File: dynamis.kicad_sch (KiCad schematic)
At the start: 189 parts, among them J0 USB_C_Receptacle_USB2.0, SW00_00 SW_Push, SW00_01 SW_Push, SW00_02 SW_Push, SW00_03 SW_Push, SW00_04 SW_Push, SW00_05 SW_Push, SW00_06 SW_Push, SW01_00 SW_Push, SW01_01 SW_Push, SW01_02 SW_Push, SW01_03 SW_Push, SW01_04 SW_Push, SW01_05 SW_Push, SW01_06 SW_Push, SW02_01 SW_Push, SW02_02 SW_Push, SW02_03 SW_Push, SW02_04 SW_Push, SW02_05 SW_Push, SW02_06 SW_Push, SW03_00 SW_Push, SW03_02 SW_Push, SW03_03 SW_Push, SW03_04 SW_Push, SW03_05 SW_Push, SW03_06 SW_Push, SW04_00 SW_Push, SW04_01 SW_Push, SW04_02 SW_Push, SW04_03 SW_Push, SW04_05 SW_Push, SW04_06 SW_Push, SW05_01 SW_Push, SW05_02 SW_Push, SW05_03 SW_Push, SW05_04 SW_Push, SW05_05 SW_Push, SW05_06 SW_Push, SW06_00 SW_Push, SW06_01 SW_Push, SW06_02 SW_Push, SW06_03 SW_Push, SW06_04 SW_Push, SW06_05 SW_Push, SW06_06 SW_Push, SW07_01 SW_Push, SW07_02 SW_Push, SW07_03 SW_Push, SW07_04 SW_Push, SW07_05 SW_Push, SW07_06 SW_Push, SW08_00 SW_Push, SW08_02 SW_Push, SW08_03 SW_Push, SW08_04 SW_Push, SW08_05 SW_Push, SW08_06 SW_Push, SW09_00 SW_Push, SW09_01 SW_Push, SW09_02 SW_Push, SW09_03 SW_Push, SW09_04 SW_Push, SW09_05 SW_Push, SW09_06 SW_Push, U0 ATmega32U4-A, U1 PMW3360DM-T2QU, U2 TLV70019DDCR, U3 74LVC1T45GW,125, U4 74LVC1T45GW,125, U5 74LVC1T45GW,125, U6 74LVC1T45GW,125, U7 74LVC1T45GW,125, Y0 16Mhz

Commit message: wip
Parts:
- added LED5, LED6: WS2812B, LED_SMD:LED_WS2812B_PLCC4_5.0x5.0mm_P3.2mm, symbol LED:WS2812B
- renumbered LED8 to LED10, LED9 to LED11, LED5 to LED7, LED6 to LED8, LED7 to LED9
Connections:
- net GND: now also LED5.3 (VSS), LED6.3 (VSS)
- net VCC: now also LED5.1 (VDD), LED6.1 (VDD)
- net at LED7.4 (DIN): now also LED6.2 (DOUT); no longer LED4.2 (DOUT)
- new net: LED4.2 (DOUT), LED5.4 (DIN)
- new net: LED5.2 (DOUT), LED6.4 (DIN)
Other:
- moved on the sheet: LED0, LED1, LED10, LED11, LED2, LED3, LED4, LED7, LED8, LED9

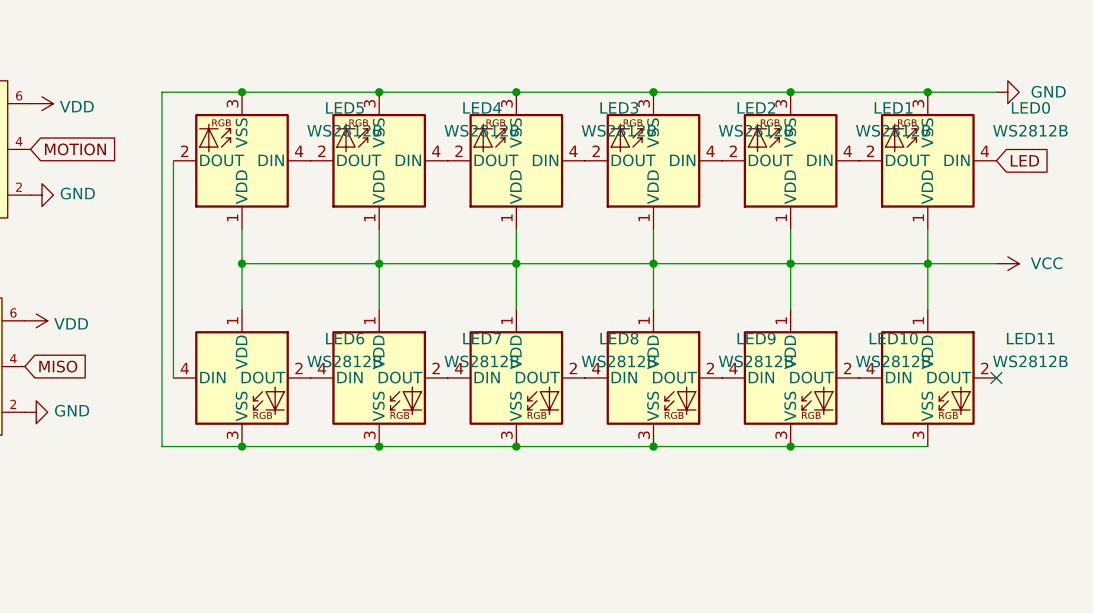
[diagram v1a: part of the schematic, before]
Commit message: mod name of 3dp gasket mount case dir
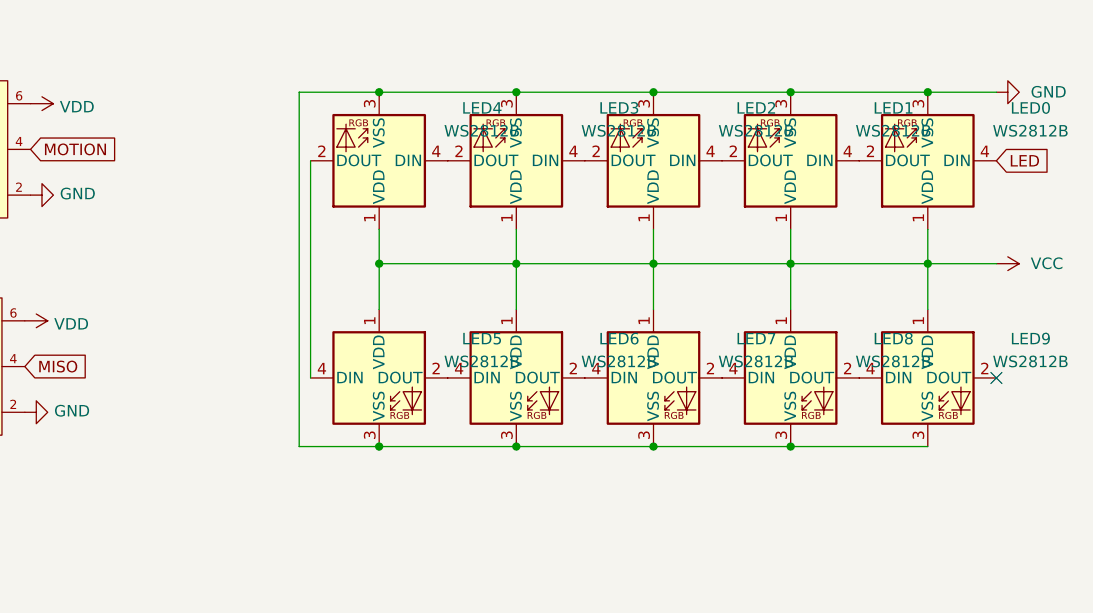
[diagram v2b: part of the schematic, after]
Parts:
- removed LED4, LED7: WS2812B, LED_SMD:LED_WS2812B_PLCC4_5.0x5.0mm_P3.2mm, symbol LED:WS2812B
- SW01_00: footprint MX_Only:MXOnly-1U-Hotswap -> MX_Only:MXOnly-1.5U-Hotswap
- SW03_00, SW04_00, SW04_01, SW04_02, SW04_06, SW09_05, SW09_06, SWSP_S04: footprint MX_Only:MXOnly-1U-Hotswap -> MX_Only:MXOnly-1.25U-Hotswap
- SW04_03: footprint MX_Only:MXOnly-1U-Hotswap -> MX_Only:MXOnly-2.25U-Hotswap-ReversedStabilizers
- SW04_05: footprint MX_Only:MXOnly-1U-Hotswap -> MX_Only:MXOnly-2.75U-Hotswap-ReversedStabilizers
- SWBS_L00: footprint MX_Only:MXOnly-1U-Hotswap -> MX_Only:MXOnly-2U-Hotswap
- SWCL_N00, SWRS_S01: footprint MX_Only:MXOnly-1U-Hotswap -> MX_Only:MXOnly-1.75U-Hotswap
- SWLS_L01: footprint MX_Only:MXOnly-1U-Hotswap -> MX_Only:MXOnly-2.25U-Hotswap
- SWRS_L01: footprint MX_Only:MXOnly-1U-Hotswap -> MX_Only:MXOnly-2.75U-Hotswap
- SWSP_L04: footprint MX_Only:MXOnly-1U-Hotswap -> MX_Only:MXOnly-6.25U-Hotswap
- renumbered LED5 to LED4, LED6 to LED5, LED8 to LED6, LED9 to LED7, LED10 to LED8, LED11 to LED9
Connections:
- net at LED6.4 (DIN): now also LED5.2 (DOUT)
- net at LED4.4 (DIN): now also LED3.2 (DOUT)
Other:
- moved on the sheet: LED4, LED5

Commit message: Develop v2 (#27)
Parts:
- removed C5, C6: 1μF, Capacitor_SMD:C_1206_3216Metric, symbol Device:C
- removed JP0: SJ, Jumper:SolderJumper-2_P1.3mm_Open_Pad1.0x1.5mm, symbol Jumper:SolderJumper_2_Open
- removed LED0, LED1, LED2, LED3, LED4, LED5, LED6, LED7, LED8, LED9: WS2812B, LED_SMD:LED_WS2812B_PLCC4_5.0x5.0mm_P3.2mm, symbol LED:WS2812B
- removed R7, R8: 10k, Resistor_SMD:R_1206_3216Metric, symbol Device:R
- removed U0: ATmega32U4-A, Package_QFP:TQFP-44_10x10mm_P0.8mm, symbol MCU_Microchip_ATmega:ATmega32U4-A
- removed U2: TLV70019DDCR, TLV70019DDCR:Texas_Instruments-TLV70019DDCR-Level_A, symbol TLV70019DDCR:TLV70019DDCR
- removed U3, U4, U5, U6, U7: 74LVC1T45GW,125, 74LVC1T45GW:Nexperia-SOT363-11_2018-0-IPC_A, symbol 74LVC1T45GW:74LVC1T45GW,125
- added C10, C12, C16, C20: 10μF, Capacitor_SMD:C_1206_3216Metric, symbol Device:C
- added C11, C13, C15, C17, C19, C9: 0.1μF, Capacitor_SMD:C_1206_3216Metric, symbol Device:C
- added C14, C18: 1μF, Capacitor_SMD:C_1206_3216Metric, symbol Device:C
- added C21: 4.7μF, Capacitor_SMD:C_1206_3216Metric, symbol Device:C
- added ESDD0: ESD5Z5V0, Diode_SMD:D_SOD-523, symbol Diode:1.5KExxA
- added F0: SMD0805-050-16V, Fuse:Fuse_1206_3216Metric, symbol Device:Fuse
- added LED00, LED01, LED02, LED03, LED04: SK6812MINI-E, SK6812MINI-E:SK6812MINIE, symbol SK6812MINI-E:SK6812MINI-E
- added R10: 63.4K, Resistor_SMD:R_1206_3216Metric, symbol Device:R
- added R11: 52.3k, Resistor_SMD:R_1206_3216Metric, symbol Device:R
- added R12: 30.1k, Resistor_SMD:R_1206_3216Metric, symbol Device:R
- added R13: 1M, Resistor_SMD:R_1206_3216Metric, symbol Device:R
- added R5: 10k, Resistor_SMD:R_1206_3216Metric, symbol Device:R
- added R9: 37.4k, Resistor_SMD:R_1206_3216Metric, symbol Device:R
- added U0: ATmega32U4-M, Package_DFN_QFN:QFN-44-1EP_7x7mm_P0.5mm_EP5.2x5.2mm, symbol MCU_Microchip_ATmega:ATmega32U4-M
- added U2, U3: TPS73601DBV, Package_TO_SOT_SMD:SOT-23-5, symbol Regulator_Linear:TPS73601DBV
- added U4: TPD4E05U06DQAR, TPD4E05U06DQAR:USON-10_L2.5-W1.0-P0.50-BL, symbol random-keyboard-parts:TPD4E05U06DQAR
- C0, C1: LCSC (none) -> C107174
- C2: LCSC (none) -> C1848
- C3: renamed from C7; LCSC (none) -> C24497
- C4: renamed from C8; LCSC (none) -> C24497
- C5: renamed from C9; LCSC (none) -> C24497
- C6: renamed from C10; LCSC (none) -> C13585
- C7: renamed from C3; LCSC (none) -> C29823
- C8: renamed from C4; LCSC (none) -> C24497
- D00_00, D00_01, D00_02, D00_03, D00_04, D00_05, D00_06, D01_00, D01_01, D01_02, D01_03, D01_04, D01_05, D01_06, D02_00, D02_01, D02_02, D02_03, D02_04, D02_05, D02_06, D03_00, D03_01, D03_02, D03_03, D03_04, D03_05, D03_06, D04_00, D04_01, D04_02, D04_03, D04_04, D04_05, D04_06, D05_00, D05_01, D05_02, D05_03, D05_04, D05_05, D05_06, D06_00, D06_01, D06_02, D06_03, D06_04, D06_05, D06_06, D07_00, D07_01, D07_02, D07_03, D07_04, D07_05, D07_06, D08_00, D08_01, D08_02, D08_03, D08_04, D08_05, D08_06, D09_00, D09_01, D09_02, D09_03, D09_04, D09_05, D09_06: LCSC (none) -> C81598
- J0: LCSC (none) -> C165948
- R0, R1: LCSC (none) -> C17958
- R2: LCSC (none) -> C17928
- R3, R4: LCSC (none) -> C964991
- R6: renamed from R5; LCSC (none) -> C17928
- R7: renamed from R6; LCSC (none) -> C286655
- RESET_SW0: LCSC (none) -> C318884
- SW00_00, SW00_01, SW00_02, SW00_03, SW00_04, SW00_05, SW00_06, SW01_00, SW01_01, SW01_02, SW01_03, SW01_04, SW01_05, SW01_06, SW02_01, SW02_02, SW02_03, SW02_04, SW02_05, SW02_06, SW03_00, SW03_02, SW03_03, SW03_04, SW03_05, SW03_06, SW04_00, SW04_01, SW04_02, SW04_03, SW04_05, SW04_06, SW05_01, SW05_02, SW05_03, SW05_04, SW05_05, SW05_06, SW06_00, SW06_01, SW06_02, SW06_03, SW06_04, SW06_05, SW06_06, SW07_01, SW07_02, SW07_03, SW07_04, SW07_05, SW07_06, SW08_00, SW08_02, SW08_03, SW08_04, SW08_05, SW08_06, SW09_00, SW09_01, SW09_02, SW09_03, SW09_04, SW09_05, SW09_06, SWBS_L00, SWBS_S00, SWCL_N00, SWCL_S00, SWET_AN00, SWLS_L01, SWLS_S01, SWRS_L01, SWRS_S01, SWSP_L04, SWSP_S04: LCSC (none) -> C5156480
- SWET_IS00: footprint MX_Only:MXOnly-1U-Hotswap -> MX_Only:MXOnly-2U-Hotswap-ReversedStabilizers; LCSC (none) -> C5156480
- Y0: footprint Crystal:Crystal_SMD_SeikoEpson_FA238-4Pin_3.2x2.5mm -> X322516MLB4SI:OSC-SMD_4P-L3.2-W2.5-BL; LCSC (none) -> C13738
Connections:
- net D+: now also U4.4 (D2+), U4.5 (D2-), U4.6 (NC), U4.7 (NC)
- net D-: now also U4.1 (D1+), U4.10 (NC), U4.2 (D1-), U4.9 (NC)
- net GND: now also C7.2, C8.2, C10.2, C11.2, C12.2, C13.2, C14.2, C16.2, C17.2, C18.2, C20.2, C21.1, C9.2, ESDD0.2 (A2), LED00.3 (GND), LED01.3 (GND), LED02.3 (GND), LED03.3 (GND), LED04.3 (GND), R10.2, R12.2, R13.1, U0.15 (GND), U0.23 (GND), U0.35 (GND), U0.43 (GND), U0.45 (GND), U0.5 (UGND), U2.2 (GND), U3.2 (GND), U4.3 (GND), U4.8 (GND); no longer C7.1, C8.1, J0.S1 (SHIELD)
- net LED: now also LED00.4 (DIN), U0.1 (PE6)
- net MISO: now also U0.11 (PB3)
- net MOSI: now also U0.10 (PB2)
- net MOTION: now also U0.12 (PB7)
- net RESET: now also R5.2, U0.13 (~{RESET})
- net RE_A: now also U0.41 (PF0)
- net RE_B: now also U0.40 (PF1)
- net SCLK: now also U0.9 (PB1)
- net VCC: now also ESDD0.1 (A1), F0.1; no longer C3.1, C4.1, C5.1, C6.1
- net col00: now also U0.18 (PD0)
- net col01: now also U0.19 (PD1)
- net col02: now also U0.37 (PF6)
- net col03: now also U0.36 (PF7)
- net col04: now also U0.22 (PD5)
- net col05: now also U0.39 (PF4)
- net col06: now also U0.38 (PF5)
- net row00: now also U0.25 (PD4)
- net row01: now also U0.26 (PD6)
- net row02: now also U0.27 (PD7)
- net row03: now also U0.21 (PD3)
- net row04: now also U0.20 (PD2)
- net row05: now also U0.31 (PC6)
- net row06: now also U0.30 (PB6)
- net row07: now also U0.29 (PB5)
- net row08: now also U0.28 (PB4)
- net row09: now also U0.32 (PC7)
- net at C2.1: now also U0.6 (UCAP)
- net at C0.2, Y0.3: now also U0.17 (XTAL1)
- net at R0.1: now also U0.4 (D+)
- net at C1.1, Y0.1: now also U0.16 (XTAL2)
- net at R2.2: now also U0.33 (~{HWB}/PE2)
- net at R1.1: now also U0.3 (D-)
- net SS renamed NCS
- net NCS: now also U0.8 (PB0)
- net VDD renamed VDD_3_3v
- net VDD_3_3v: now also C11.1, C12.1, C19.1, C20.1, R11.1, U3.5 (OUT); no longer R7.1, U1.4 (VDD)
- new net: C15.2, R10.1, R9.2, U2.4 (FB)
- new net: C19.2, R11.2, R12.1, U3.4 (FB)
- new net: C7.1, C8.1, U1.3 (VDDPIX)
- new net: LED03.2 (DOUT), LED04.4 (DIN)
- new net: LED02.2 (DOUT), LED03.4 (DIN)
- new net: LED01.2 (DOUT), LED02.4 (DIN)
- new net: LED00.2 (DOUT), LED01.4 (DIN)
- new net +5V: C13.1, C14.1, C17.1, C18.1, C3.1, C4.1, C5.1, C6.1, F0.2, LED00.1 (VDD), LED01.1 (VDD), LED02.1 (VDD), LED03.1 (VDD), LED04.1 (VDD), R5.1, U0.14 (VCC), U0.2 (UVCC), U0.24 (AVCC), U0.34 (VCC), U0.44 (AVCC), U0.7 (VBUS), U2.1 (IN), U2.3 (EN), U3.1 (IN), U3.3 (EN)
- new net GNDPWR: C21.2, J0.S1 (SHIELD), R13.2
- new net VDD_SS: C10.1, C15.1, C16.1, C9.1, R7.1, R9.1, U1.4 (VDD), U2.5 (OUT)
- no-connect marks 10 -> 9
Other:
- note added: "BADGE LED"
- note added: "Controller"
- note added: "ESD"
- note added: "Encoder"
- note added: "KEY MATRIX"
- note added: "PMW3360"
- title: (none) -> dynamis
- moved on the sheet: C0, C1, C2, C3, C4, C5, C6, C7, C8, D00_00, D00_01, D00_02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
